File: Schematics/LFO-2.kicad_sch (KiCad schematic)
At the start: 82 parts, among them J100 Conn_01x04, J95 Conn_01x03, J96 Conn_01x03, J97 Conn_01x03, J98 Conn_01x10h, J99 Conn_01x05, Q14 BSS138, Q15 BSS138, U100 AMS1117-3.3, U101 SSI2130, U95 LM324, U96 LM324, U97 PCF8574, U99 LM78L05

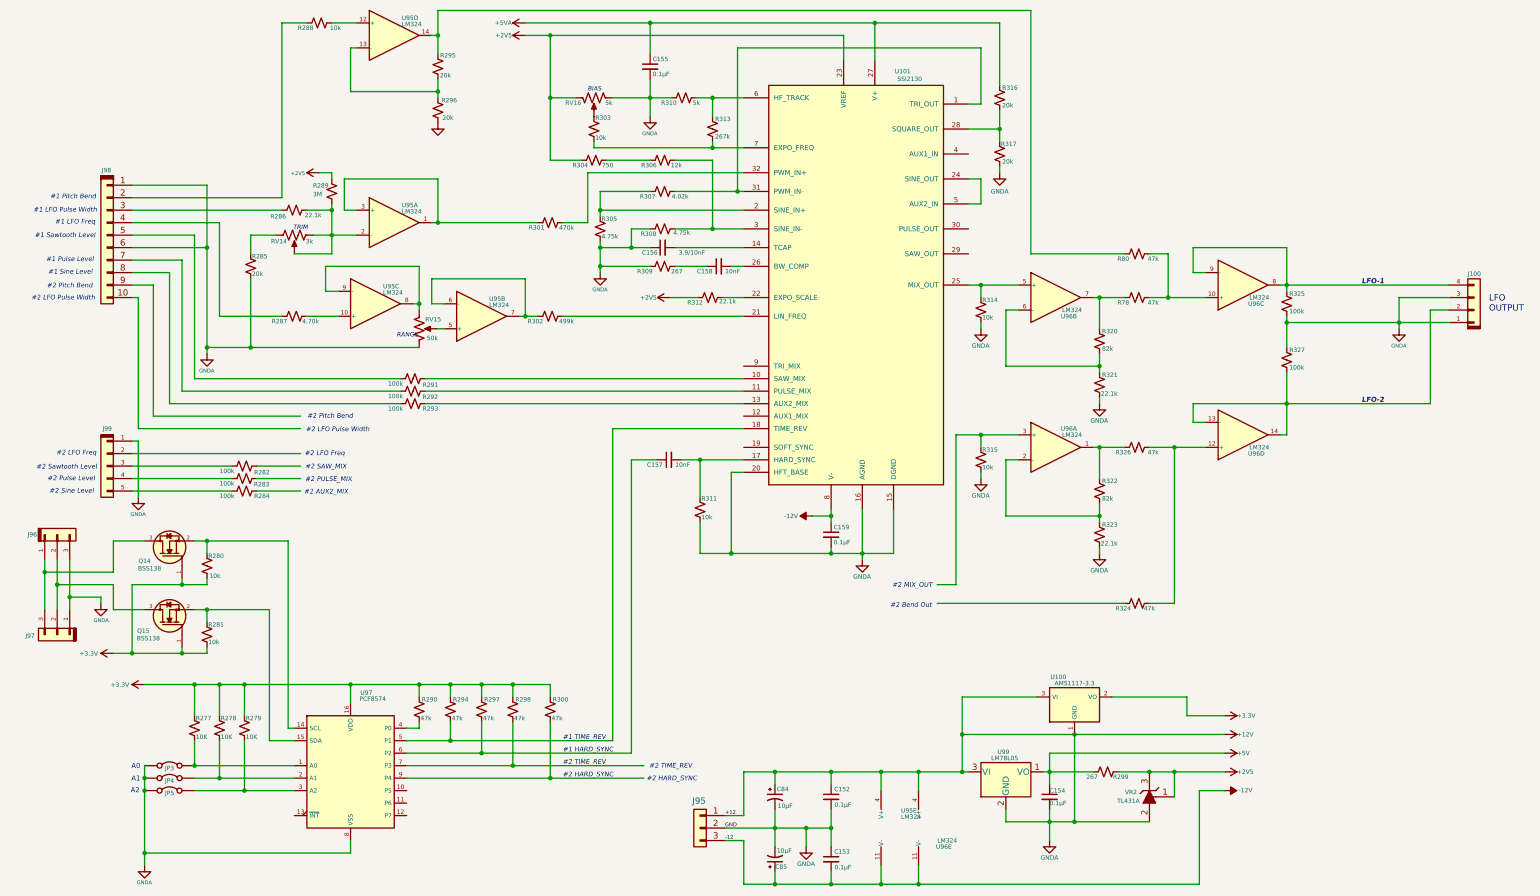
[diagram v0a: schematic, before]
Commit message: Fixed bugs in voice selection on configuration.  Reorganized schematics to have different master drawings for power and audio paths.  Started work on dual 3-pole state variable filter with resonance.
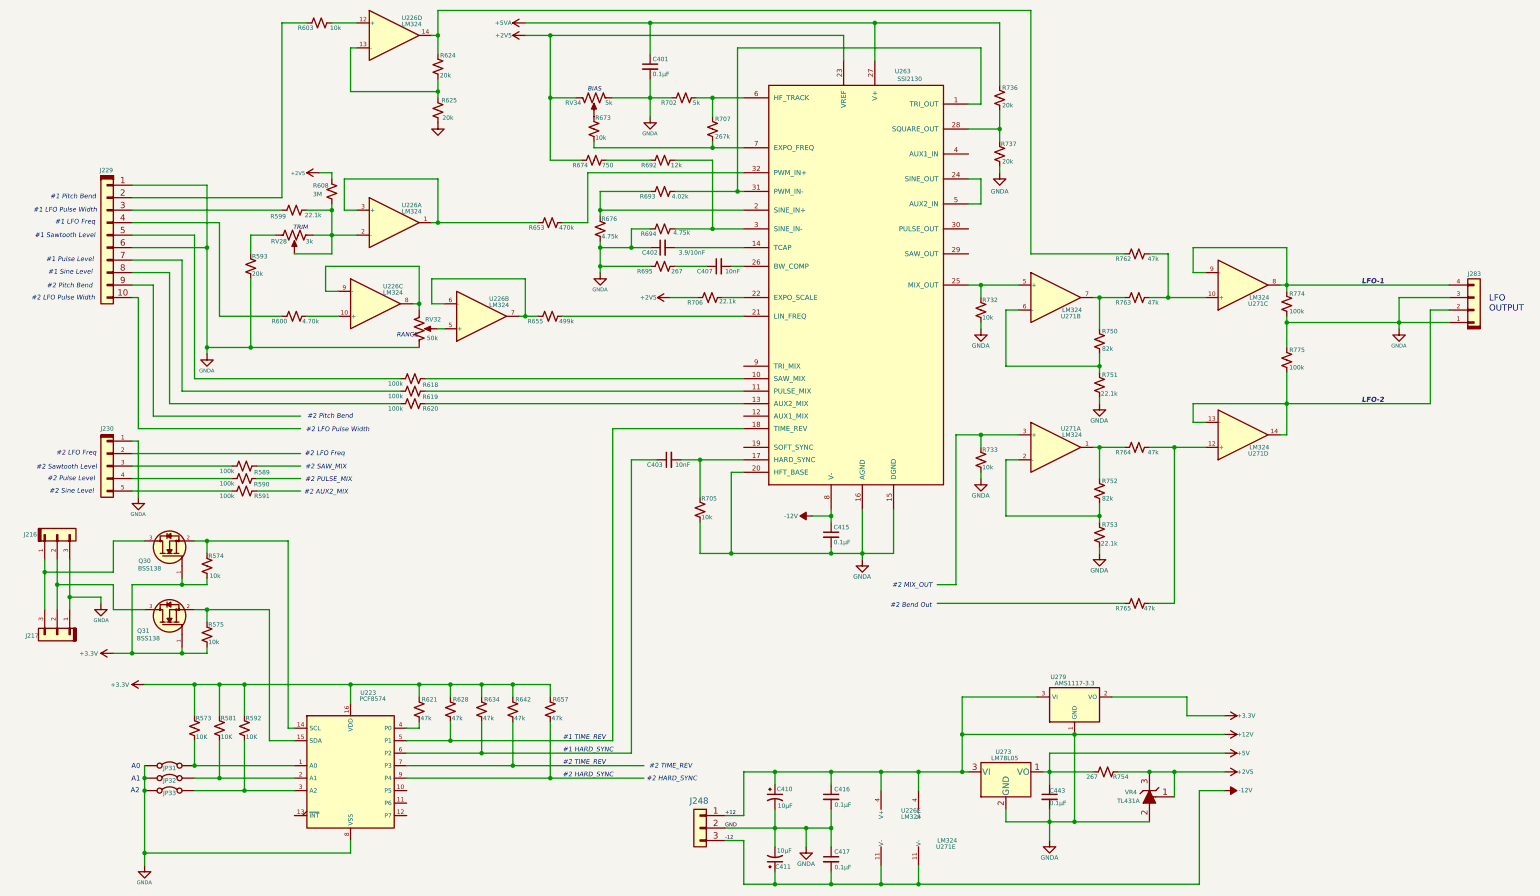
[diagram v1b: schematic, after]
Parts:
- renumbered C155 to C401, C156 to C402, C157 to C403, C158 to C407, C84 to C410, C85 to C411, C159 to C415, C152 to C416, C153 to C417, C154 to C443, J96 to J216, J97 to J217, J98 to J229, J99 to J230, J95 to J248, J100 to J283, JP3 to JP31, JP4 to JP32, JP5 to JP33, Q14 to Q30, Q15 to Q31, R277 to R573, R280 to R574, R281 to R575, R278 to R581, R282 to R589, R283 to R590, R284 to R591, R279 to R592, R285 to R593, R286 to R599, R287 to R600, R288 to R603, R289 to R608, R291 to R618, R292 to R619, R293 to R620, R290 to R621, R295 to R624, R296 to R625, R294 to R628, R297 to R634, R298 to R642, R301 to R653, R302 to R655, R300 to R657, R303 to R673, R304 to R674, R305 to R676, R306 to R692, R307 to R693, R308 to R694, R309 to R695, R310 to R702, R311 to R705, R312 to R706, R313 to R707, R314 to R732, R315 to R733, R316 to R736, R317 to R737, R320 to R750, R321 to R751, R322 to R752, R323 to R753, R299 to R754, R80 to R762, R78 to R763, R326 to R764, R324 to R765, R325 to R774, R327 to R775, RV14 to RV28, RV15 to RV32, RV16 to RV34, U97 to U223, U95 to U226, U101 to U263, U96 to U271, U99 to U273, U100 to U279, VR2 to VR4

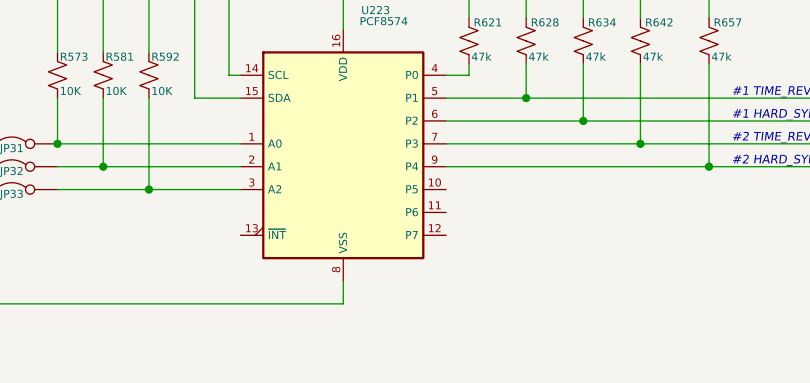
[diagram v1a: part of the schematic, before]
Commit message: New output mixer with VCAs
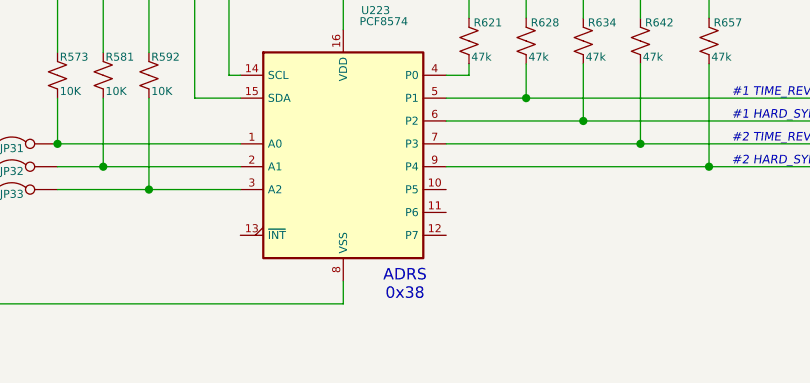
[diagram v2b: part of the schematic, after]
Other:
- note added: "ADRS 0x38"
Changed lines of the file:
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@@
+		)
+	)
+	(text "ADRS\n0x38"
+		(exclude_from_sim no)
+		(at 89.408 184.658 0)
+		(effects
+			(font
+				(size 1.27 1.27)
+			)
 		)
 	)
